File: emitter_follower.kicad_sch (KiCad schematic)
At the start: 14 parts, among them Q4001 DNLS350E, Q4002 DPLS350E, Q4003 TIP41C, Q4004 TIP42C

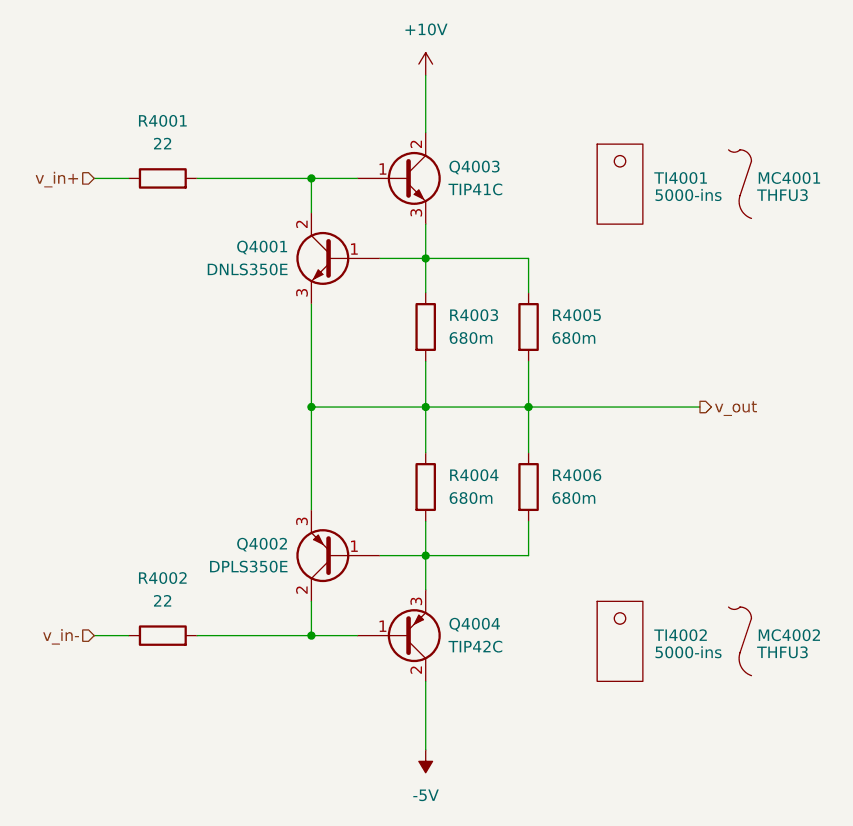
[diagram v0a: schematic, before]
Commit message: add outstage separation by connectors for individual PCB
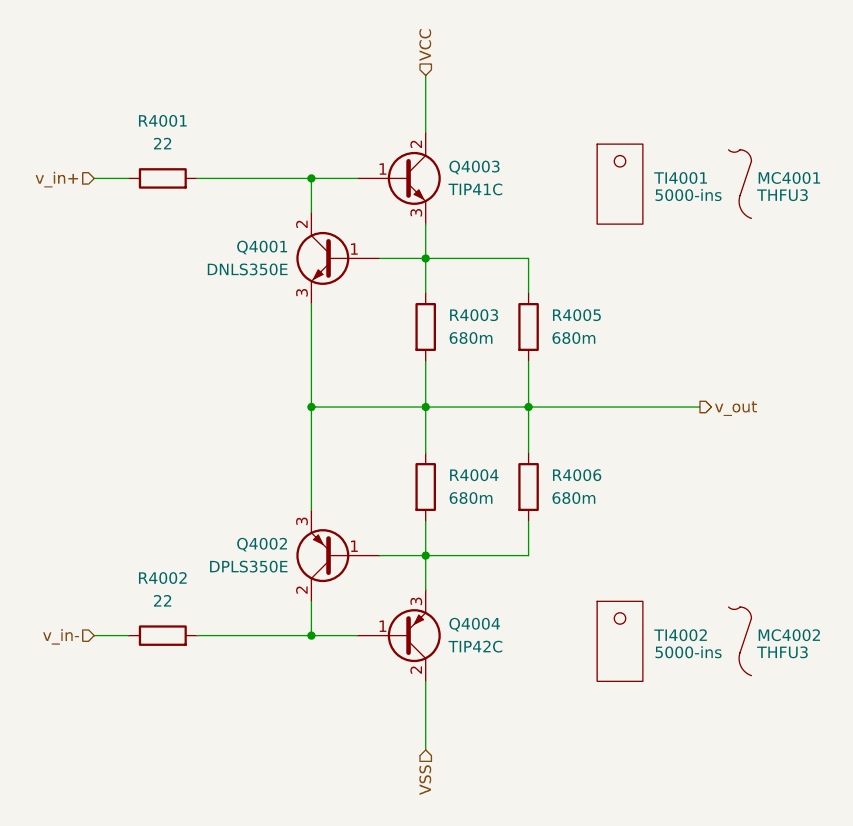
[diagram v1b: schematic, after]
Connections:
- net +10V renamed VCC
- net -5V renamed VSS

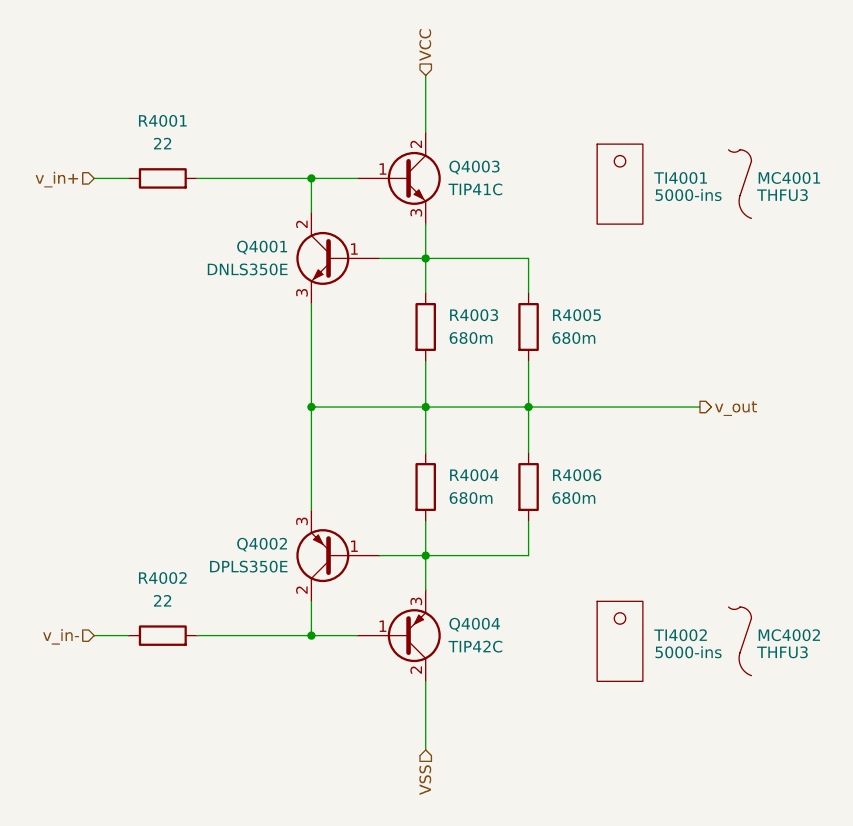
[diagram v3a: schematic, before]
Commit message: edit pss footprint library: export all footprints to library 'pss' and update footprint links
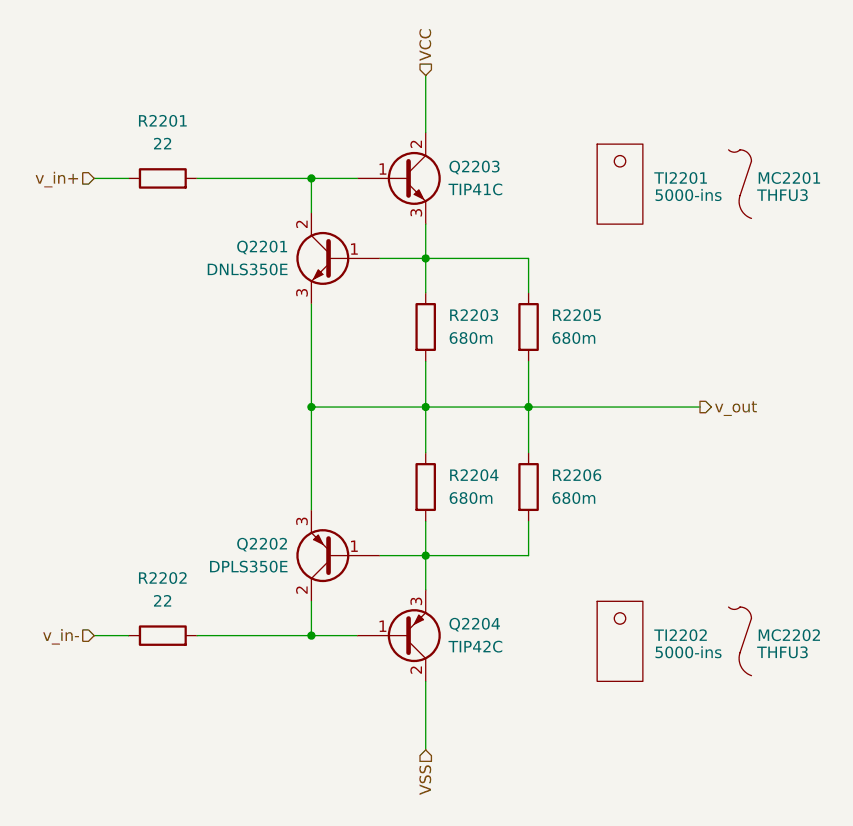
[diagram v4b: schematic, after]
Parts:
- Q2201: renamed from Q4001; footprint Package_TO_SOT_SMD:SOT-223-3_TabPin2 -> pss:SOT-223-3_TabPin2
- Q2202: renamed from Q4002; footprint Package_TO_SOT_SMD:SOT-223-3_TabPin2 -> pss:SOT-223-3_TabPin2
- Q2203: renamed from Q4003; footprint Package_TO_SOT_THT:TO-220-3_Vertical -> pss:TO-220-3_Vertical
- Q2204: renamed from Q4004; footprint Package_TO_SOT_THT:TO-220-3_Vertical -> pss:TO-220-3_Vertical
- R2201: renamed from R4001; footprint Resistor_THT:R_Axial_DIN0617_L17.0mm_D6.0mm_P20.32mm_Horizontal -> pss:R_Axial_DIN0617_L17.0mm_D6.0mm_P20.32mm_Horizontal
- R2202: renamed from R4002; footprint Resistor_THT:R_Axial_DIN0617_L17.0mm_D6.0mm_P20.32mm_Horizontal -> pss:R_Axial_DIN0617_L17.0mm_D6.0mm_P20.32mm_Horizontal
- R2203: renamed from R4003; footprint Resistor_THT:R_Axial_DIN0411_L9.9mm_D3.6mm_P12.70mm_Horizontal -> pss:R_Axial_DIN0411_L9.9mm_D3.6mm_P12.70mm_Horizontal
- R2204: renamed from R4004; footprint Resistor_THT:R_Axial_DIN0411_L9.9mm_D3.6mm_P12.70mm_Horizontal -> pss:R_Axial_DIN0411_L9.9mm_D3.6mm_P12.70mm_Horizontal
- R2205: renamed from R4005; footprint Resistor_THT:R_Axial_DIN0411_L9.9mm_D3.6mm_P12.70mm_Horizontal -> pss:R_Axial_DIN0411_L9.9mm_D3.6mm_P12.70mm_Horizontal
- R2206: renamed from R4006; footprint Resistor_THT:R_Axial_DIN0411_L9.9mm_D3.6mm_P12.70mm_Horizontal -> pss:R_Axial_DIN0411_L9.9mm_D3.6mm_P12.70mm_Horizontal
- renumbered MC4001 to MC2201, MC4002 to MC2202, TI4001 to TI2201, TI4002 to TI2202
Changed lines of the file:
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@@
 		(dnp no)
 		(fields_autoplaced yes)
-		(property "Reference" "R4001"
+		(property "Reference" "R2201"
 			(at 130.81 68.58 90)
 			(effects
@@
 			)
 		)
-		(property "Footprint" "Resistor_THT:R_Axial_DIN0617_L17.0mm_D6.0mm_P20.32mm_Horizontal"
+		(property "Footprint" "pss:R_Axial_DIN0617_L17.0mm_D6.0mm_P20.32mm_Horizontal"
 			(at 130.81 76.708 90)
 			(effects
@@
 		(dnp no)
 		(fields_autoplaced yes)
-		(property "Reference" "R4002"
+		(property "Reference" "R2202"
 			(at 130.81 119.38 90)
 			(effects
@@
 			)
 		)
-		(property "Footprint" "Resistor_THT:R_Axial_DIN0617_L17.0mm_D6.0mm_P20.32mm_Horizontal"
+		(property "Footprint" "pss:R_Axial_DIN0617_L17.0mm_D6.0mm_P20.32mm_Horizontal"
 			(at 130.81 127.508 90)
 			(effects
@@
 		(dnp no)
 		(fields_autoplaced yes)
-		(property "Reference" "MC4002"
+		(property "Reference" "MC2202"
 			(at 196.85 125.7299 0)
 			(effects
@@
 		(dnp no)
 		(fields_autoplaced yes)
-		(property "Reference" "R4004"
+		(property "Reference" "R2204"
 			(at 162.56 107.9499 0)
 			(effects
@@
 			)
 		)
-		(property "Footprint" "Resistor_THT:R_Axial_DIN0411_L9.9mm_D3.6mm_P12.70mm_Horizontal"
+		(property "Footprint" "pss:R_Axial_DIN0411_L9.9mm_D3.6mm_P12.70mm_Horizontal"
 			(at 158.242 109.22 90)
 			(effects
@@
 		(dnp no)
 		(fields_autoplaced yes)
-		(property "Reference" "R4006"
+		(property "Reference" "R2206"
 			(at 173.99 107.9499 0)
 			(effects
@@
 			)
 		)
-		(property "Footprint" "Resistor_THT:R_Axial_DIN0411_L9.9mm_D3.6mm_P12.70mm_Horizontal"
+		(property "Footprint" "pss:R_Axial_DIN0411_L9.9mm_D3.6mm_P12.70mm_Horizontal"
 			(at 169.672 109.22 90)
 			(effects
@@
 		(dnp no)
 		(fields_autoplaced yes)
-		(property "Reference" "R4005"
+		(property "Reference" "R2205"
 			(at 173.99 90.1699 0)
 			(effects
@@
 			)
 		)
-		(property "Footprint" "Resistor_THT:R_Axial_DIN0411_L9.9mm_D3.6mm_P12.70mm_Horizontal"
+		(property "Footprint" "pss:R_Axial_DIN0411_L9.9mm_D3.6mm_P12.70mm_Horizontal"
 			(at 169.672 91.44 90)
 			(effects
@@
 		(on_board yes)
 		(dnp no)
-		(property "Reference" "Q4002"
+		(property "Reference" "Q2202"
 			(at 144.78 115.5699 0)
 			(effects
@@
 			)
 		)
-		(property "Footprint" "Package_TO_SOT_SMD:SOT-223-3_TabPin2"
+		(property "Footprint" "pss:SOT-223-3_TabPin2"
 			(at 143.51 114.935 0)
 			(effects
@@
 		(dnp no)
 		(fields_autoplaced yes)
-		(property "Reference" "Q4003"
+		(property "Reference" "Q2203"
 			(at 162.56 73.6599 0)
 			(effects
@@
 			)
 		)
-		(property "Footprint" "Package_TO_SOT_THT:TO-220-3_Vertical"
+		(property "Footprint" "pss:TO-220-3_Vertical"
 			(at 163.83 76.835 0)
 			(effects
@@
 		(dnp no)
 		(fields_autoplaced yes)
-		(property "Reference" "TI4002"
+		(property "Reference" "TI2202"
 			(at 185.42 125.7299 0)
 			(effects
@@
 		(on_board yes)
 		(dnp no)
-		(property "Reference" "Q4001"
+		(property "Reference" "Q2201"
 			(at 144.78 82.5499 0)
 			(effects
@@
 			)
 		)
-		(property "Footprint" "Package_TO_SOT_SMD:SOT-223-3_TabPin2"
+		(property "Footprint" "pss:SOT-223-3_TabPin2"
 			(at 143.51 85.725 0)
 			(effects
@@
 		(dnp no)
 		(fields_autoplaced yes)
-		(property "Reference" "TI4001"
+		(property "Reference" "TI2201"
 			(at 185.42 74.9299 0)
 			(effects
@@
 		(dnp no)
 		(fields_autoplaced yes)
-		(property "Reference" "R4003"
+		(property "Reference" "R2203"
 			(at 162.56 90.1699 0)
 			(effects
@@
 			)
 		)
-		(property "Footprint" "Resistor_THT:R_Axial_DIN0411_L9.9mm_D3.6mm_P12.70mm_Horizontal"
+		(property "Footprint" "pss:R_Axial_DIN0411_L9.9mm_D3.6mm_P12.70mm_Horizontal"
 			(at 158.242 91.44 90)
 			(effects
@@
 		(dnp no)
 		(fields_autoplaced yes)
-		(property "Reference" "Q4004"
+		(property "Reference" "Q2204"
 			(at 162.56 124.4599 0)
 			(effects
@@
 			)
 		)
-		(property "Footprint" "Package_TO_SOT_THT:TO-220-3_Vertical"
+		(property "Footprint" "pss:TO-220-3_Vertical"
 			(at 163.83 123.825 0)
 			(effects
@@
 		(dnp no)
 		(fields_autoplaced yes)
-		(property "Reference" "MC4001"
+		(property "Reference" "MC2201"
 			(at 196.85 74.9299 0)
 			(effects
